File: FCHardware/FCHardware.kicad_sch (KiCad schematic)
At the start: 20 parts, among them J1 XT60Male, J2 Conn_01x03, J3 Conn_01x03, J4 Conn_01x03, J5 Conn_01x03, U1 ESC_Xrotor_65A_4in1, U4 TPS629203, U5 MPU-6050

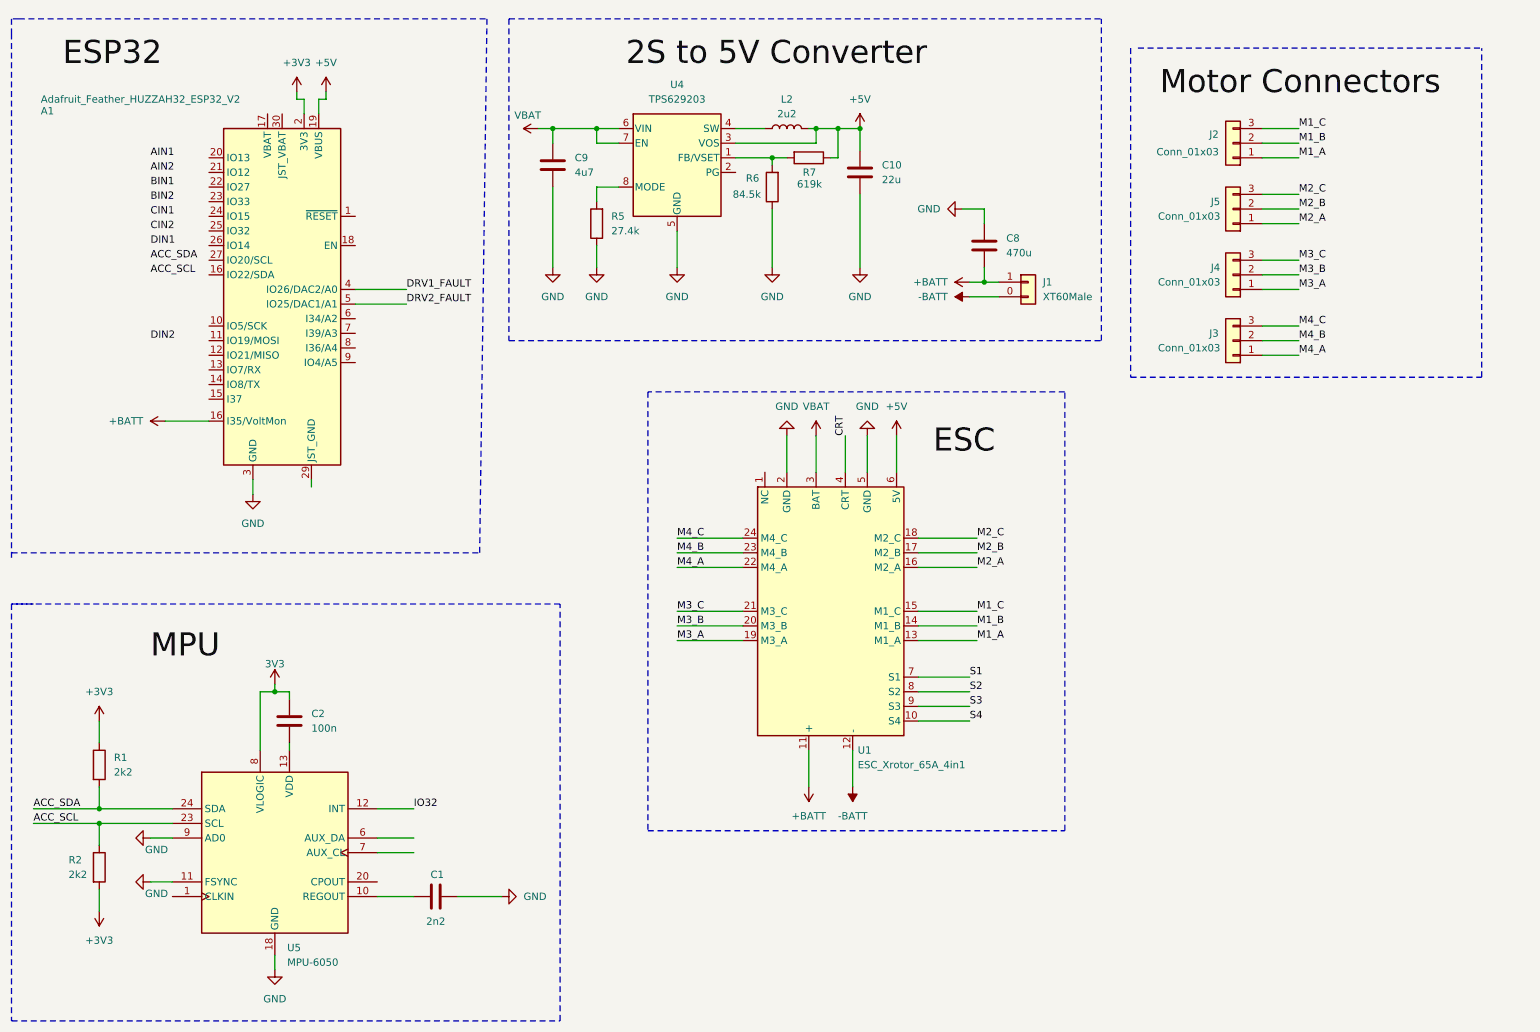
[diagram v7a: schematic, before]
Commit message: Fixed mismatch in ESC piout, removed connectors, wired ESC
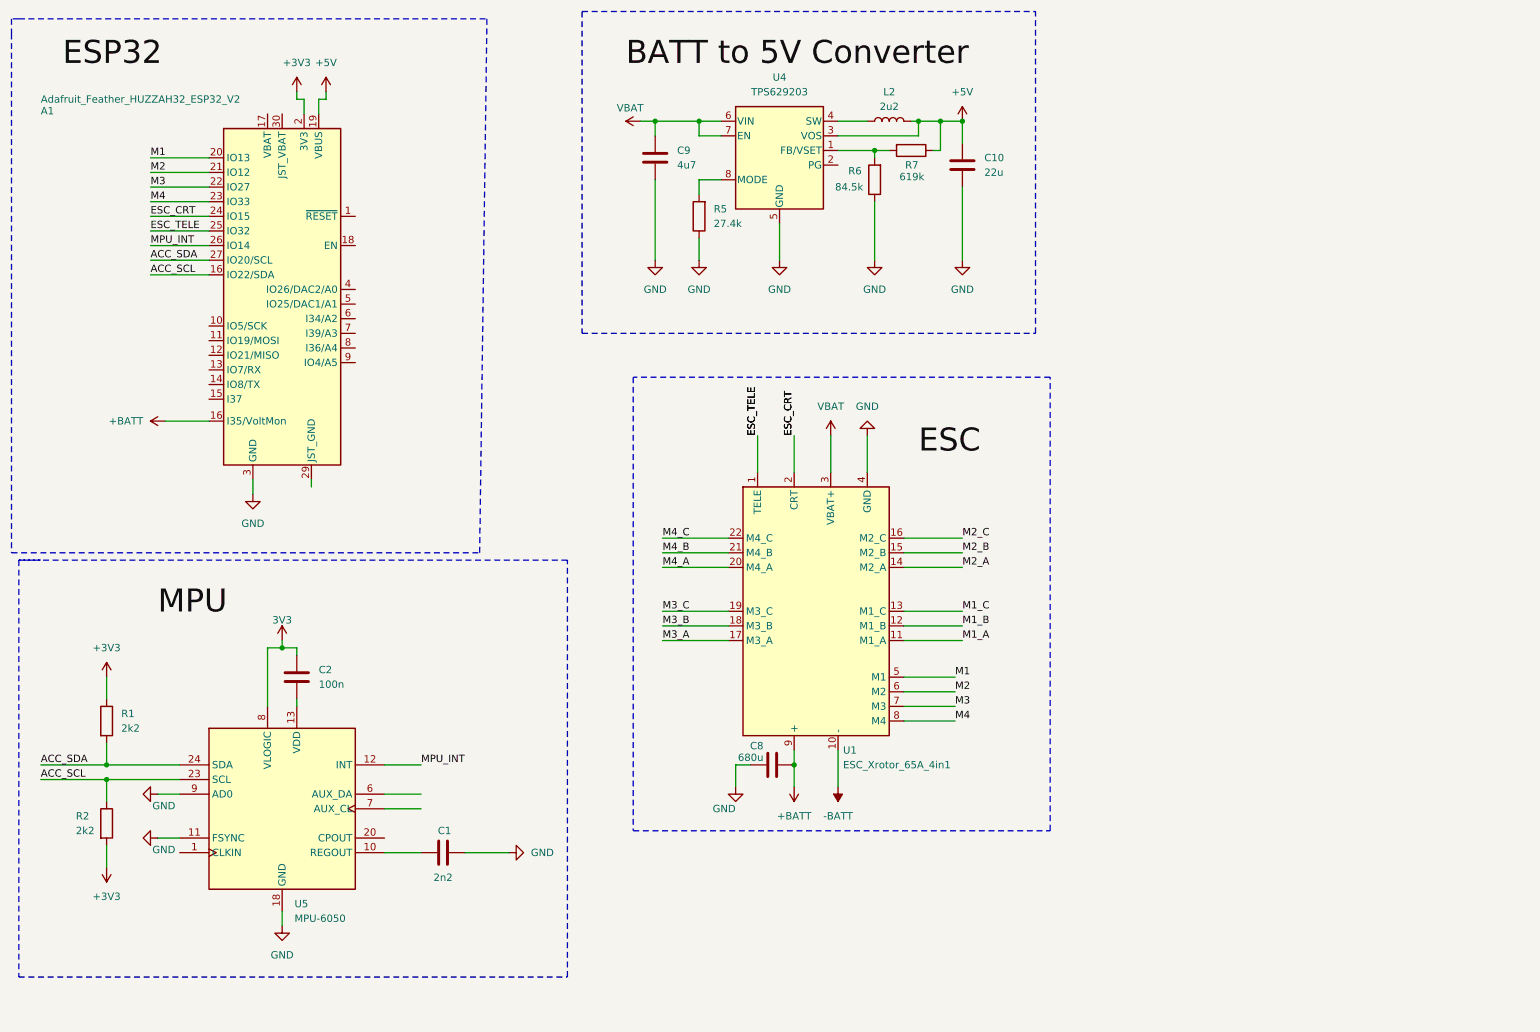
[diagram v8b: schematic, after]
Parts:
- removed J1: XT60Male, symbol Custom_ESP32_Library:XT60Male
- removed J2, J3, J4, J5: Conn_01x03, symbol Connector_Generic:Conn_01x03
- C8: value 470u -> 680u
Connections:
- net CRT is gone; now on net GND: U1.4 (GND)
- net IO32 is gone; now on net MPU_INT: U5.12 (INT)
- net S1 is gone; now on net M3: U1.7 (M3)
- net S2 is gone; now on net M4: U1.8 (M4)
- net S3 is gone; now on net +BATT: U1.9 (+)
- net S4 is gone; now on net -BATT: U1.10 (-)
- net +5V: no longer U1.6 (5V)
- net +BATT: no longer U1.11 (+)
- net -BATT: no longer U1.12 (-)
- net ACC_SCL: now also A1.16 (I35/VoltMon)
- net ACC_SDA: now also A1.27 (IO20/SCL)
- net GND: no longer U1.2 (GND), U1.5 (GND)
- net M1_A: now also U1.11 (M1_A); no longer U1.13 (M1_A)
- net M1_B: now also U1.12 (M1_B); no longer U1.14 (M1_B)
- net M1_C: now also U1.13 (M1_C); no longer U1.15 (M1_C)
- net M2_A: now also U1.14 (M2_A); no longer U1.16 (M2_A)
- net M2_B: now also U1.15 (M2_B); no longer U1.17 (M2_B)
- net M2_C: now also U1.16 (M2_C); no longer U1.18 (M2_C)
- net M3_A: now also U1.17 (M3_A); no longer U1.19 (M3_A)
- net M3_B: now also U1.18 (M3_B); no longer U1.20 (M3_B)
- net M3_C: now also U1.19 (M3_C); no longer U1.21 (M3_C)
- net M4_A: now also U1.20 (M4_A); no longer U1.22 (M4_A)
- net M4_B: now also U1.21 (M4_B); no longer U1.23 (M4_B)
- net M4_C: now also U1.22 (M4_C); no longer U1.24 (M4_C)
- net ESC_TELE: now reaches U1.1 (TELE)
- net ESC_TELE: now also A1.25 (IO32)
- net M1: now reaches A1.20 (IO13)
- net M1: now also U1.5 (M1)
- net M2: now reaches A1.21 (IO12)
- net M2: now also U1.6 (M2)
- net M3: now reaches A1.22 (IO27)
- net M4: now reaches A1.23 (IO33)
- net ESC_CRT: now reaches A1.24 (IO15)
- net ESC_CRT: now also U1.2 (CRT)
- net MPU_INT: now reaches A1.26 (IO14)
- net DRV1_FAULT: no longer names the net of A1.4 (IO26/DAC2/A0)
- net DRV2_FAULT: no longer names the net of A1.5 (IO25/DAC1/A1)
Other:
- moved on the sheet: C1, C10, C2, C8, C9, L2, R1, R2, R5, R6, R7, U4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
